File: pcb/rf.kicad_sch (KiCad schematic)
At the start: 9 parts, among them U5 CAM-M8Q-0, U6 W3012, U7 E22-900MM22S

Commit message: ufl
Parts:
- added R14: 0R, Resistor_SMD:R_0603_1608Metric, symbol Device:R
- added U8: BWU.FL-IPEX1, Rocketry_Easyeda:IPEX-SMD_BWIPX-1-001E, symbol Rocketry_Easyeda:BWU.FL-IPEX1
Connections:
- net GND: now also U8.2, U8.3
- net at C46.1, R31.1, U6.1 (ANT): now also R14.2
- new net: R14.1, U8.1

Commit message: added active gps antenna connector
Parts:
- added C13: 47pF, Capacitor_SMD:C_0603_1608Metric_Pad1.08x0.95mm_HandSolder, symbol Device:C
- added L3: 27nH, Inductor_SMD:L_0603_1608Metric_Pad1.05x0.95mm_HandSolder, symbol Device:L
- added R16, R17: 0R, Resistor_SMD:R_0603_1608Metric_Pad0.98x0.95mm_HandSolder, symbol Device:R
- added U12: BWU.FL-IPEX1, Rocketry_Easyeda:IPEX-SMD_BWIPX-1-001E, symbol Rocketry_Easyeda:BWU.FL-IPEX1
- C28, C46: footprint Capacitor_SMD:C_0603_1608Metric -> Capacitor_SMD:C_0603_1608Metric_Pad1.08x0.95mm_HandSolder
- R14, R31: footprint Resistor_SMD:R_0603_1608Metric -> Resistor_SMD:R_0603_1608Metric_Pad0.98x0.95mm_HandSolder
- U6: footprint Rocketry_Manual:W3012-ANT-PKG-Mirrored -> Rocketry_Manual:W3012-ANT-PKG
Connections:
- net GND: now also U12.2, U12.3
- net at C28.1, R31.2, U7.6 (ANT): now also R14.2
- net at C46.1, R31.1, U6.1 (ANT): no longer R14.2
- net at U5.17 (RF_IN): now also R16.1, R17.1; no longer U5.16 (RF_OUT)
- new net: C13.1, L3.2, U12.1
- new net: C13.2, R16.2
- new net: R17.2, U5.16 (RF_OUT)
- new net +3.3VA: L3.1
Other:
- moved on the sheet: R14, U8

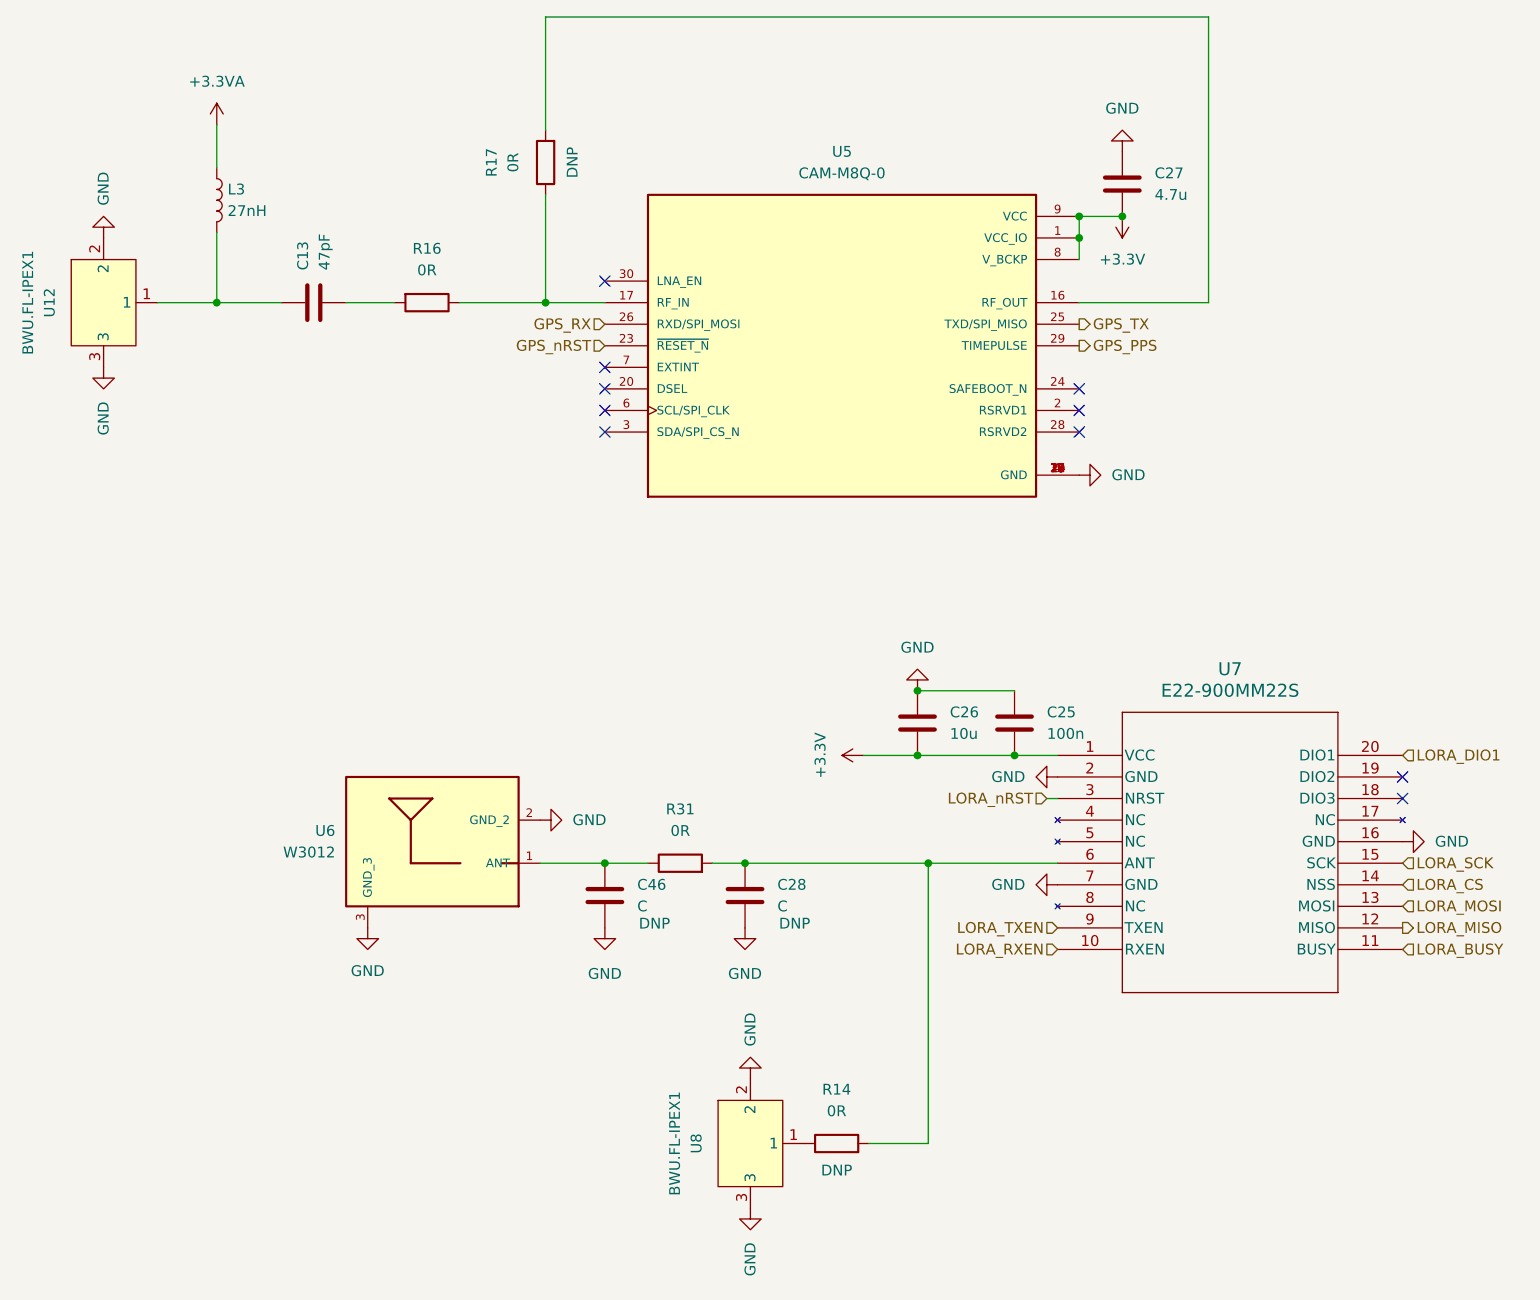
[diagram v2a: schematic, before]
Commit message: add pull up resistor for sd, change pad net
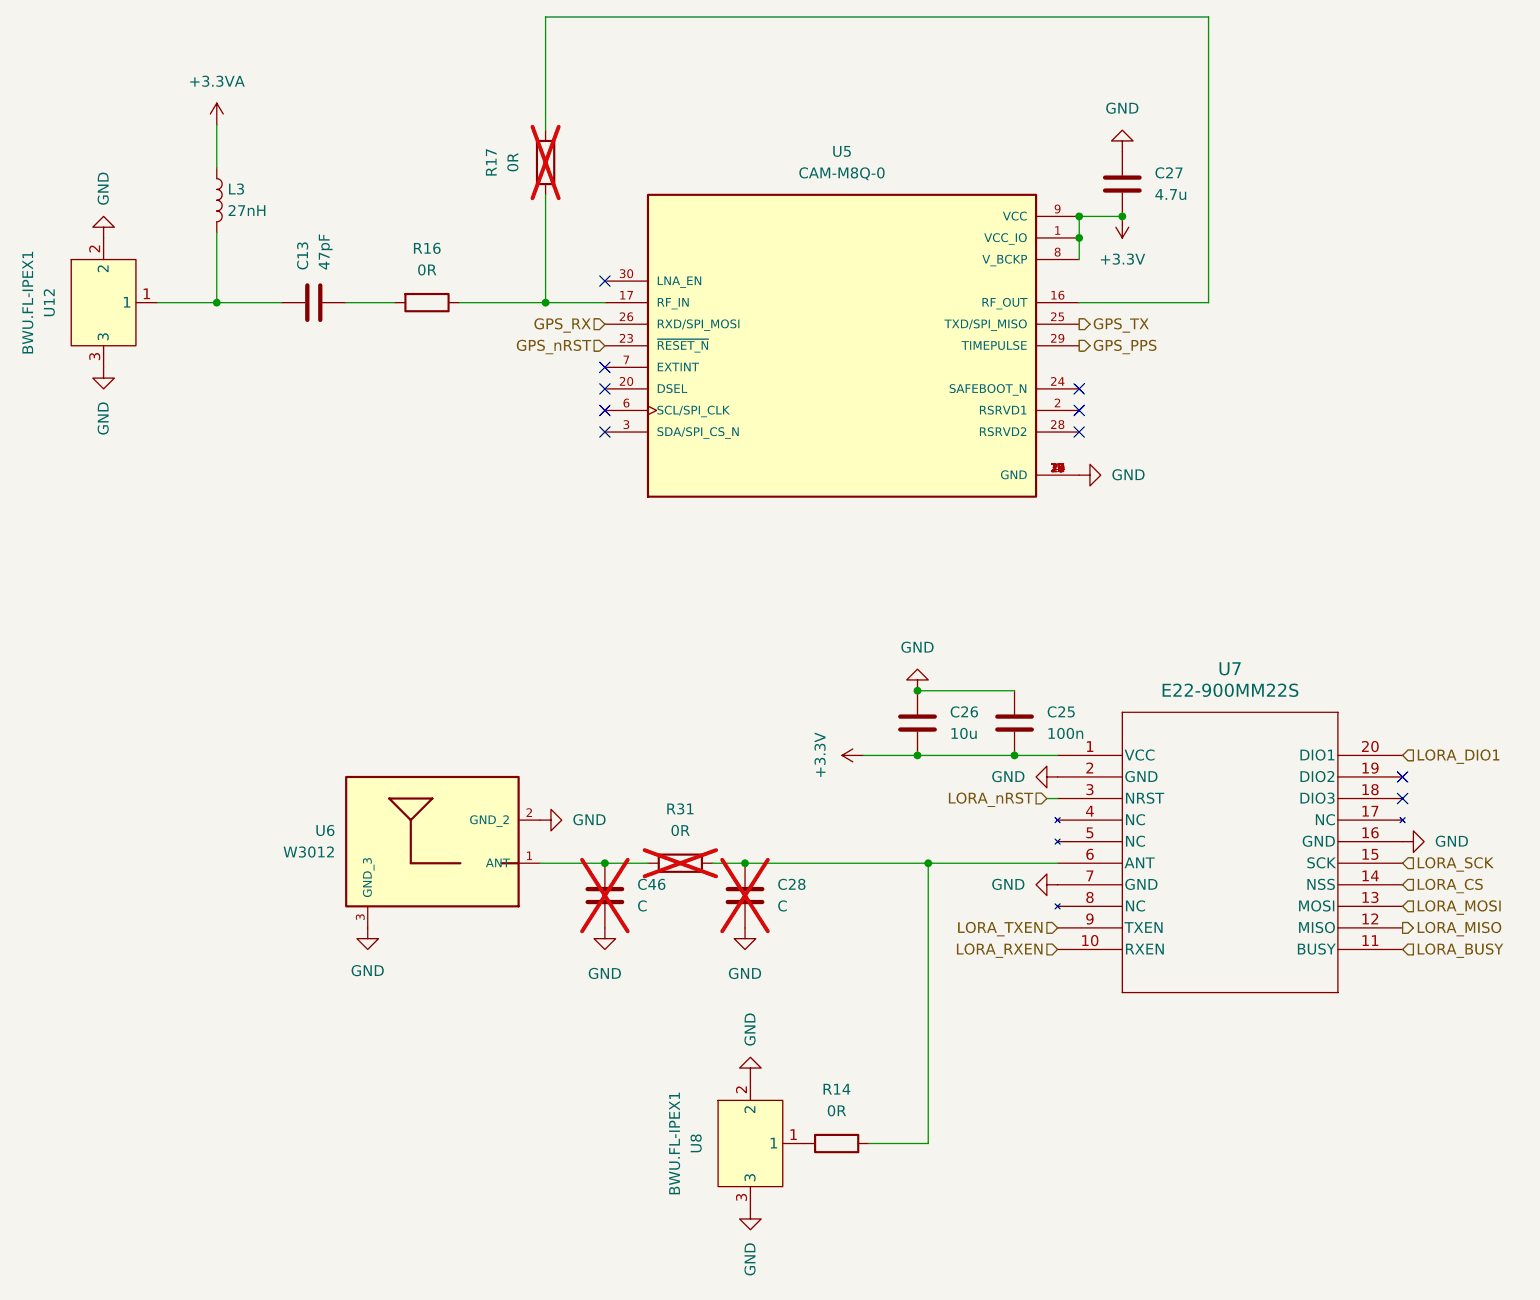
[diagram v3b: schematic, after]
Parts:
- C28, C46, R17: DNP DNP -> (none); now not fitted
- R14: DNP DNP -> (none)
- R31: now not fitted
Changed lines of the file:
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@@
 		(in_bom yes)
 		(on_board yes)
-		(dnp no)
+		(dnp yes)
 		(property "Reference" "C28"
 			(at 114.3 137.1599 0)
@@
 				)
 				(hide yes)
-			)
-		)
-		(property "DNP" "DNP"
-			(at 116.332 141.732 0)
-			(effects
-				(font
-					(size 1.27 1.27)
-				)
 			)
 		)
@@
 		(in_bom yes)
 		(on_board yes)
-		(dnp no)
+		(dnp yes)
 		(property "Reference" "R17"
 			(at 80.645 52.07 90)
@@
 				)
 				(hide yes)
-			)
-		)
-		(property "DNP" "DNP"
-			(at 90.17 52.07 90)
-			(effects
-				(font
-					(size 1.27 1.27)
-				)
 			)
 		)
@@
 		(in_bom yes)
 		(on_board yes)
-		(dnp no)
+		(dnp yes)
 		(fields_autoplaced yes)
 		(property "Reference" "R31"
@@
 		(in_bom yes)
 		(on_board yes)
-		(dnp no)
+		(dnp yes)
 		(property "Reference" "C46"
 			(at 97.79 137.1599 0)
@@
 				)
 				(hide yes)
-			)
-		)
-		(property "DNP" "DNP"
-			(at 99.822 141.732 0)
-			(effects
-				(font
-					(size 1.27 1.27)
-				)
 			)
 		)
@@
 			)
 		)
-		(property "DNP" "DNP"
-			(at 121.285 170.815 90)
-			(effects
-				(font
-					(size 1.27 1.27)
-				)
-			)
-		)
